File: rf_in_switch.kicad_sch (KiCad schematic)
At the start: 6 parts, among them P17 CONUFL001-SMD-T, P18 CONUFL001-SMD-T, U31 QPC1022TR7, U32 QPC1022TR7

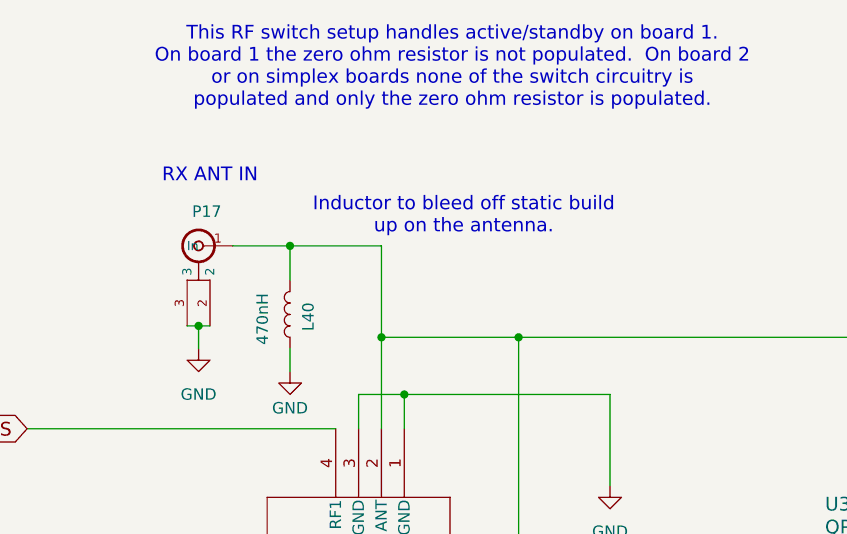
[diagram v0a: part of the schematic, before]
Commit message: More cleanups on the filtering
Signed-off-by: Corey Minyard <corey@minyard.net>
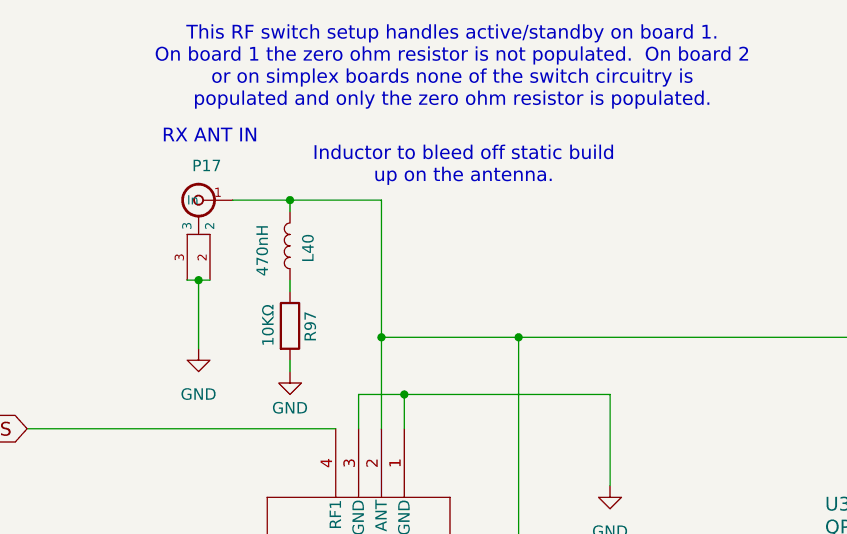
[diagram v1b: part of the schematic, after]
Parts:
- added R97: 10KΩ, Resistor_SMD:R_0402_1005Metric_Pad0.72x0.64mm_HandSolder, symbol Device:R
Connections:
- net GND: now also R97.2; no longer L40.2
- new net: L40.2, R97.1
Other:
- moved on the sheet: L40, P17
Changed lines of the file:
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@@
 	(text "Inductor to bleed off static build\nup on the antenna."
 		(exclude_from_sim no)
-		(at 115.824 55.118 0)
+		(at 115.824 49.53 0)
 		(effects
 			(font
@@
 	(text "RX ANT IN"
 		(exclude_from_sim no)
-		(at 82.296 51.562 0)
+		(at 82.296 47.244 0)
 		(effects
 			(font
@@
 	)
 	(junction
-		(at 96.52 58.42)
+		(at 96.52 53.34)
 		(diameter 0)
 		(color 0 0 0 0)
@@
 	)
 	(junction
+		(at 86.36 62.23)
+		(diameter 0)
+		(color 0 0 0 0)
+	)
+	(junction
 		(at 121.92 68.58)
 		(diameter 0)
@@
 		(color 0 0 0 0)
 	)
-	(junction
-		(at 86.36 67.31)
-		(diameter 0)
-		(color 0 0 0 0)
+	(wire
+		(pts
+			(xy 96.52 71.12) (xy 96.52 72.39)
+		)
+		(stroke
+			(width 0)
+			(type default)
+		)
 	)
 	(wire
@@
 	(wire
 		(pts
-			(xy 86.36 67.31) (xy 86.36 69.85)
-		)
-		(stroke
-			(width 0)
-			(type default)
-		)
-	)
-	(wire
-		(pts
 			(xy 163.83 55.88) (xy 162.56 55.88)
 		)
@@
 	(wire
 		(pts
-			(xy 86.36 67.31) (xy 85.09 67.31)
+			(xy 86.36 62.23) (xy 85.09 62.23)
 		)
 		(stroke
@@
 	(wire
 		(pts
-			(xy 86.36 67.31) (xy 87.63 67.31)
+			(xy 86.36 62.23) (xy 86.36 69.85)
+		)
+		(stroke
+			(width 0)
+			(type default)
+		)
+	)
+	(wire
+		(pts
+			(xy 86.36 62.23) (xy 87.63 62.23)
 		)
 		(stroke
@@
 	(wire
 		(pts
-			(xy 106.68 58.42) (xy 106.68 68.58)
+			(xy 106.68 53.34) (xy 106.68 68.58)
 		)
 		(stroke
@@
 	(wire
 		(pts
-			(xy 96.52 58.42) (xy 96.52 62.23)
-		)
-		(stroke
-			(width 0)
-			(type default)
-		)
-	)
-	(wire
-		(pts
 			(xy 99.06 120.65) (xy 139.7 120.65)
 		)
@@
 	(wire
 		(pts
-			(xy 90.17 58.42) (xy 96.52 58.42)
+			(xy 90.17 53.34) (xy 96.52 53.34)
 		)
 		(stroke
@@
 	(wire
 		(pts
-			(xy 96.52 58.42) (xy 106.68 58.42)
+			(xy 96.52 53.34) (xy 106.68 53.34)
+		)
+		(stroke
+			(width 0)
+			(type default)
+		)
+	)
+	(wire
+		(pts
+			(xy 96.52 53.34) (xy 96.52 54.61)
 		)
 		(stroke
@@
 	(wire
 		(pts
-			(xy 96.52 69.85) (xy 96.52 72.39)
+			(xy 96.52 62.23) (xy 96.52 63.5)
 		)
 		(stroke
@@
 	)
 	(symbol
+		(lib_id "Device:R")
+		(at 96.52 67.31 0)
+		(unit 1)
+		(exclude_from_sim no)
+		(in_bom yes)
+		(on_board yes)
+		(dnp no)
+		(property "Reference" "R97"
+			(at 98.806 69.088 90)
+			(effects
+				(font
+					(size 1.27 1.27)
+				)
+				(justify left)
+			)
+		)
+		(property "Value" "10KΩ"
+			(at 94.107 69.596 90)
+			(effects
+				(font
+					(size 1.27 1.27)
+				)
+				(justify left)
+			)
+		)
+		(property "Footprint" "Resistor_SMD:R_0402_1005Metric_Pad0.72x0.64mm_HandSolder"
+			(at 94.742 67.31 90)
+			(effects
+				(font
+					(size 1.27 1.27)
+				)
+				(hide yes)
+			)
+		)
+		(property "Datasheet" "~"
+			(at 96.52 67.31 0)
+			(effects
+				(font
+					(size 1.27 1.27)
+				)
+			)
+		)
+		(property "Description" ""
+			(at 96.52 67.31 0)
+			(effects
+				(font
+					(size 1.27 1.27)
+				)
+			)
+		)
+		(pin "1"
+		)
+		(pin "2"
+		)
+		(instances
+			(project "PacSat_AFSK"
+				(path "/cc9f42d2-6985-41ac-acab-5ab7b01c5b38/4fa888af-703c-49ed-93bb-d56d2f02c470/64a91b23-a882-4658-bea9-c6c8274e2ac4"
+					(reference "R97")
+					(unit 1)
+				)
+			)
+		)
+	)
+	(symbol
 		(lib_id "PACSAT_DEV_misc:U_FL")
-		(at 86.36 58.42 0)
+		(at 86.36 53.34 0)
 		(mirror y)
 		(unit 1)
@@
 		(dnp no)
 		(property "Reference" "P17"
-			(at 88.9 54.61 0)
+			(at 88.9 49.53 0)
 			(effects
 				(font
@@
 		)
 		(property "Value" "CONUFL001-SMD-T"
-			(at 86.36 58.42 0)
+			(at 86.36 53.34 0)
 			(effects
 				(font
@@
 		)
 		(property "Footprint" "PacSatDev_misc:CONN1_CONUFL_TEC"
-			(at 86.36 58.42 0)
+			(at 86.36 53.34 0)
 			(effects
 				(font
@@
 		)
 		(property "Datasheet" ""
-			(at 86.36 58.42 0)
+			(at 86.36 53.34 0)
 			(effects
 				(font
@@
 		)
 		(property "Description" ""
-			(at 86.36 58.42 0)
+			(at 86.36 53.34 0)
 			(effects
 				(font
@@
 	(symbol
 		(lib_id "Device:L")
-		(at 96.52 66.04 0)
+		(at 96.52 58.42 0)
 		(mirror y)
 		(unit 1)
@@
 		(dnp no)
 		(property "Reference" "L40"
-			(at 98.552 66.294 90)
+			(at 98.552 58.674 90)
 			(effects
 				(font
@@
 		)
 		(property "Value" "470nH"
-			(at 93.472 66.548 90)
+			(at 93.472 58.928 90)
 			(effects
 				(font
@@
 		)
 		(property "Footprint" "Inductor_SMD:L_0805_2012Metric_Pad1.05x1.20mm_HandSolder"
-			(at 96.52 66.04 0)
+			(at 96.52 58.42 0)
 			(effects
 				(font
@@
 		)
 		(property "Datasheet" "~"
-			(at 96.52 66.04 0)
+			(at 96.52 58.42 0)
 			(effects
 				(font
@@
 		)
 		(property "Description" ""
-			(at 96.52 66.04 0)
-			(effects
-				(font
+			(at 96.52 58.42 0)
+			(effects
+				(font

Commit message: Track and doc cleanups
Signed-off-by: Corey Minyard <corey@minyard.net>
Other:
- note added: "This RF switch setup handles RX active/standby. On board 1 the zero ohm resistor is not populated. On board 2 or on simplex boards none of the switch circuitry is populated and only the zero ohm resistor is populated."
- note removed: "This RF switch setup handles active/standby on board 1. On board 1 the zero ohm resistor is not populated. On board 2 or on simplex boards none of the switch circuitry is populated and only the zero ohm resistor is populated."
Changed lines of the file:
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@@
 		)
 	)
-	(text "This RF switch setup handles active/standby on board 1.\nOn board 1 the zero ohm resistor is not populated.  On board 2\nor on simplex boards none of the switch circuitry is\npopulated and only the zero ohm resistor is populated."
+	(text "This RF switch setup handles RX active/standby.\nOn board 1 the zero ohm resistor is not populated.  On board 2\nor on simplex boards none of the switch circuitry is\npopulated and only the zero ohm resistor is populated."
 		(exclude_from_sim no)
 		(at 114.554 38.608 0)

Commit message: Have the BOM file fixer output xls, not csv
The omega symbol gets translated properly from xls.

Signed-off-by: Corey Minyard <corey@minyard.net>
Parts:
- R96: value 0 -> 0Ω
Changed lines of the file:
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@@
 			)
 		)
-		(property "Value" "0"
+		(property "Value" "0Ω"
 			(at 123.698 100.203 0)
 			(effects

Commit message: Added some docs and notes about various things
Signed-off-by: Corey Minyard <corey@minyard.net>
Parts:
- R96: now left out of the parts list
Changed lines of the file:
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@@
 		(unit 1)
 		(exclude_from_sim no)
-		(in_bom yes)
+		(in_bom no)
 		(on_board yes)
 		(dnp yes)

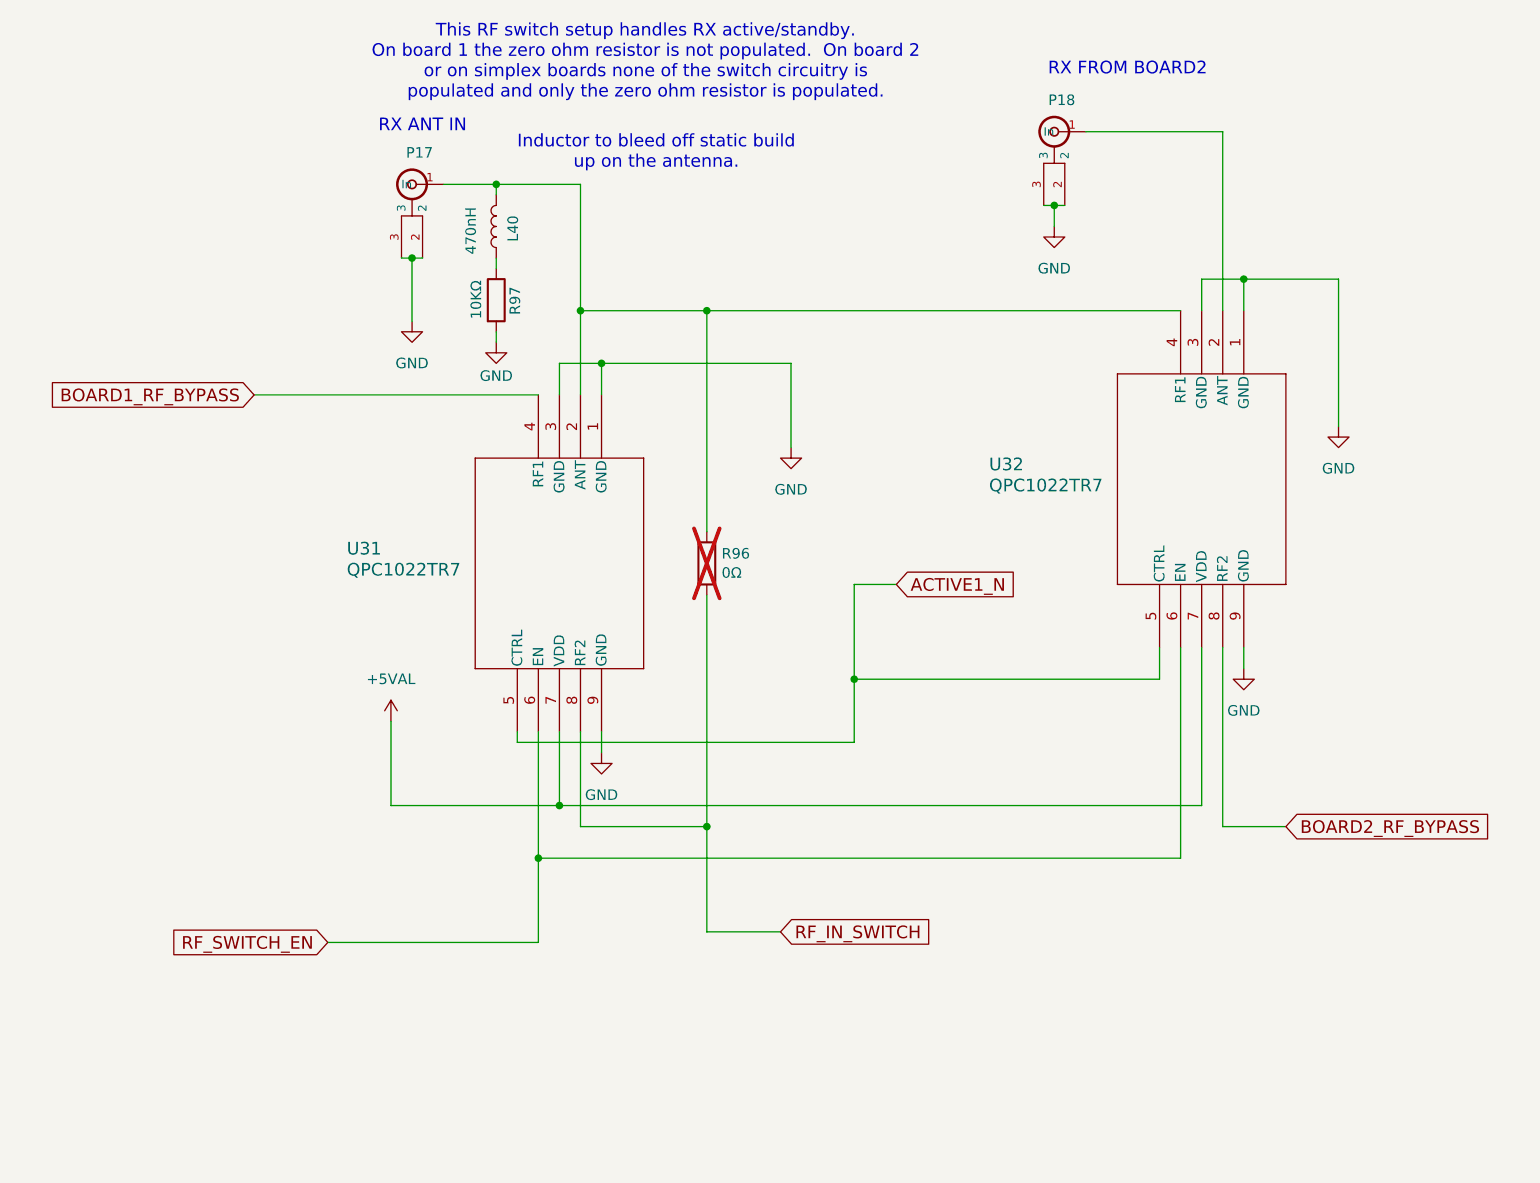
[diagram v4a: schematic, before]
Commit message: Fix a bug in the RF switch circuitry
The board bypass circuitry had an error, the board1 in and antenna
connections were flipped on the switch.  Put them in the right place.

Signed-off-by: Corey Minyard <corey@minyard.net>
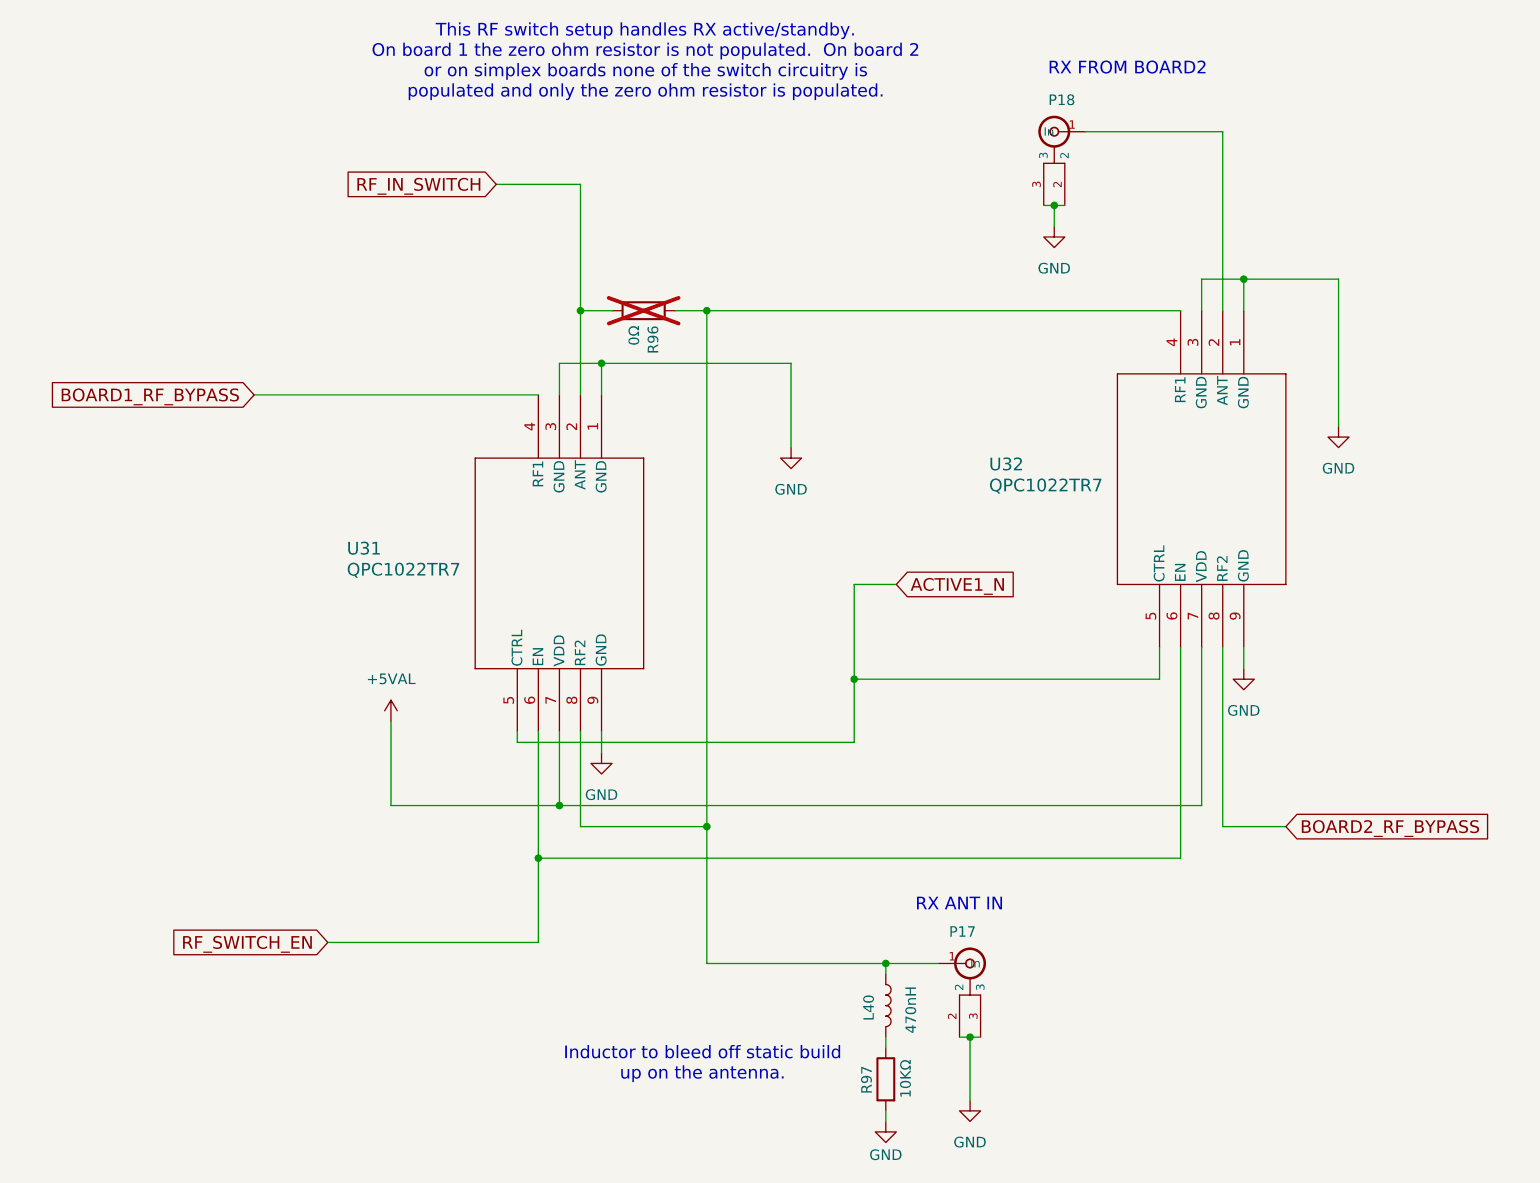
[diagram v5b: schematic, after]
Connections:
- net RF_IN_SWITCH: now also U31.2 (ANT); no longer U31.8 (RF2)
- net at L40.1, P17.1 (In), R96.1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: now also U31.8 (RF2); no longer U31.2 (ANT)
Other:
- moved on the sheet: L40, P17, R96, R97
